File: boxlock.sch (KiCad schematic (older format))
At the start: 38 parts, among them J2 SOLENOID, J3 USB_B, J4 VEXT, J6 CONN_02X05, J8 KEYPAD, Q1 TIP120, Q2 TIP120, SW1 RESET, U1 LD1117AS33TR, U2 NE555, U3 SAMD21E

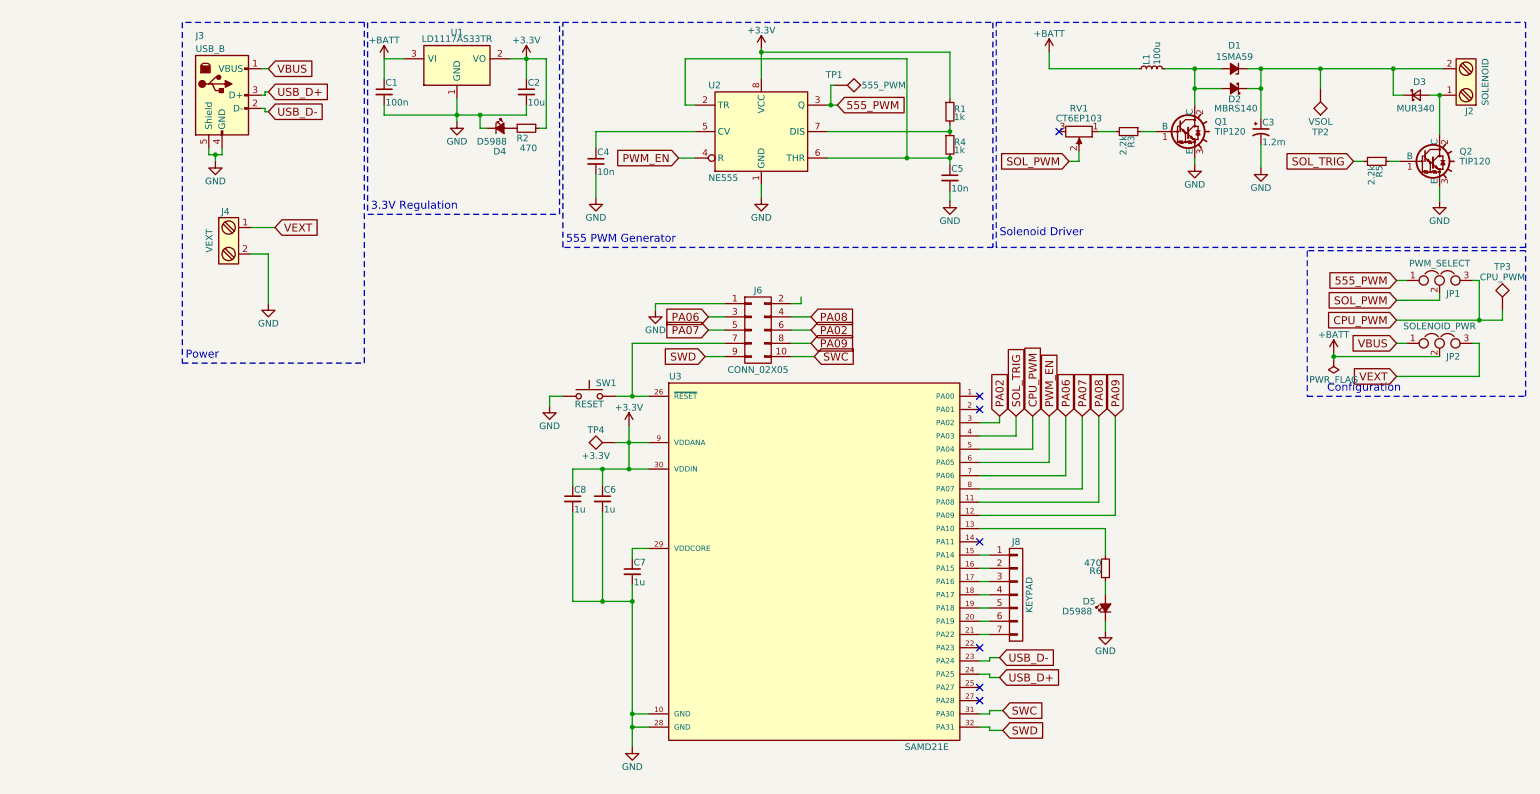
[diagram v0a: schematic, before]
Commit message: Relayout for rev 1.1.
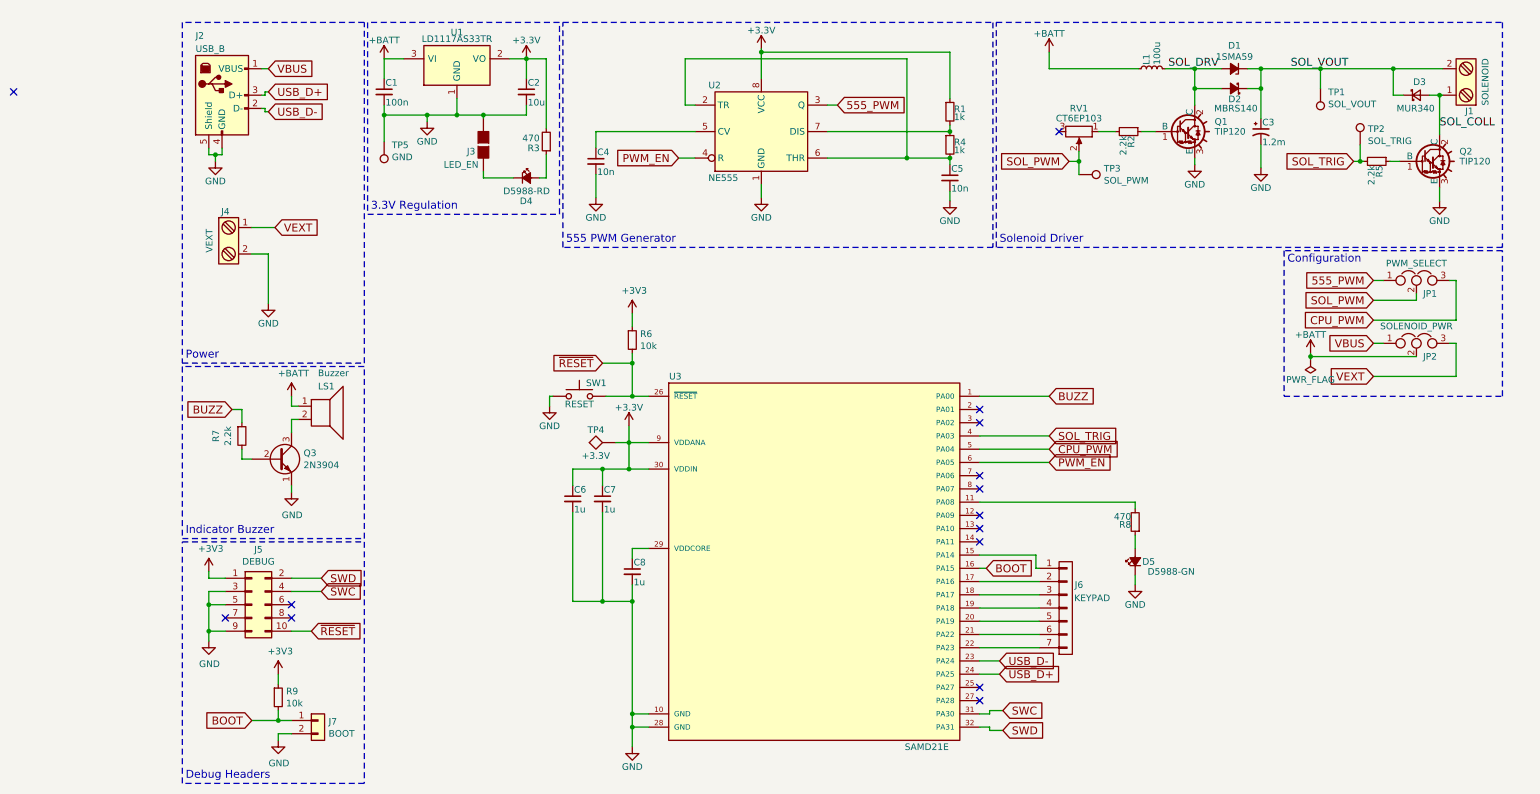
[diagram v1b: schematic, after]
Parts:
- removed J6: CONN_02X05, Pin_Headers:Pin_Header_Straight_2x05_Pitch2.54mm, symbol boxlock-rescue:CONN_02X05-RESCUE-boxlock
- removed TP1: 555_PWM, Measurement_Points:Test_Point_Keystone_5005-5009_Compact, symbol boxlock-rescue:TEST-RESCUE-boxlock
- removed TP2: VSOL, Measurement_Points:Test_Point_Keystone_5005-5009_Compact, symbol boxlock-rescue:TEST-RESCUE-boxlock
- removed TP3: CPU_PWM, Measurement_Points:Test_Point_Keystone_5005-5009_Compact, symbol boxlock-rescue:TEST-RESCUE-boxlock
- added J3: LED_EN, Connectors:GS2, symbol Connector:GS2
- added J5: DEBUG, Pin_Headers:Pin_Header_Straight_2x05_Pitch1.27mm, symbol Connector:Conn_02x05_Odd_Even
- added J7: BOOT, Pin_Headers:Pin_Header_Straight_1x02_Pitch2.54mm, symbol Connector:Conn_01x02
- added LS1: Buzzer, footprints:CEP-2242, symbol device:Speaker
- added Q3: 2N3904, TO_SOT_Packages_THT:TO-92_Molded_Narrow, symbol Transistor:2N3904
- added R6, R9: 10k, Resistors_SMD:R_0805_HandSoldering, symbol device:R_Small
- added R7: 2.2k, Resistors_SMD:R_0805_HandSoldering, symbol device:R_Small
- added TP1: SOL_VOUT, Measurement_Points:Test_Point_Keystone_5005-5009_Compact, symbol Connector:Test_Point
- added TP2: SOL_TRIG, Measurement_Points:Test_Point_Keystone_5005-5009_Compact, symbol Connector:Test_Point
- added TP3: SOL_PWM, Measurement_Points:Test_Point_Keystone_5005-5009_Compact, symbol Connector:Test_Point
- added TP5: GND, Measurement_Points:Test_Point_Keystone_5005-5009_Compact, symbol Connector:Test_Point
- D4: value D5988 -> D5988-RD
- D5: value D5988 -> D5988-GN
- J2: renamed from J3; footprint Connectors:USB_Micro-B -> footprints:USB_Micro-B-circular
- renumbered C8 to C6, C6 to C7, C7 to C8, J2 to J1, J8 to J6, R3 to R2, R2 to R3, R6 to R8
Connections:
- net PA08 is gone; now on an unnamed net: U3.11 (PA08)
- net +3V3: now also R3.2, J5.1 (Pin_1), R6.1, R9.1; no longer R3.1
- net +BATT: now also LS1.1
- net GND: now also J3.2 (G2), J5.3 (Pin_3), J5.5 (Pin_5), J5.9 (Pin_9), J7.2 (Pin_2), Q3.1 (E), TP5.1; no longer D4.1 (K)
- net SOL_PWM: now also TP3.1
- net SOL_TRIG: now also TP2.1
- net SWC: now also J5.4 (Pin_4)
- net SWD: now also J5.2 (Pin_2)
- net SOL_VOUT: now reaches C3.1, D1.1 (K), D2.1 (K), D3.1 (K), J1.2
- net SOL_VOUT: now also TP1.1
- net SOL_COLL: now reaches D3.2 (A), J1.1, Q2.2 (C)
- net SOL_DRV: now reaches D1.2 (A), D2.2 (A), L1.2, Q1.2 (C)
- net ~RESET: now reaches SW1.2, U3.26 (~RESET~)
- net ~RESET: now also J5.10 (Pin_10), R6.2
- net BUZZ: now reaches U3.1 (PA00)
- net BUZZ: now also R7.1
- net at R8.2: no longer U3.13 (PA10)
- net at J6.2 (P2): now also U3.17 (PA16); no longer U3.16 (PA15)
- net at J6.3 (P3): now also U3.18 (PA17); no longer U3.17 (PA16)
- net at J6.4 (P4): now also U3.19 (PA18); no longer U3.18 (PA17)
- net at J6.5 (P5): now also U3.20 (PA19); no longer U3.19 (PA18)
- net at J6.6 (P6): now also U3.21 (PA22); no longer U3.20 (PA19)
- net at J6.7 (P7): now also U3.22 (PA23); no longer U3.21 (PA22)
- net at D4.2 (A): now also R3.1; no longer R3.2
- net PA02: no longer names the net of U3.3 (PA02)
- net PA06: no longer names the net of U3.7 (PA06)
- net PA07: no longer names the net of U3.8 (PA07)
- net PA09: no longer names the net of U3.12 (PA09)
- new net: D4.1 (K), J3.1 (G1)
- new net: LS1.2, Q3.3 (C)
- new net: Q3.2 (B), R7.2
- new net BOOT: J7.1 (Pin_1), R9.2, U3.16 (PA15)
- no-connect marks 7 -> 14
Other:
- note added: "Debug Headers"
- note added: "Indicator Buzzer"
- moved on the sheet: D4, D5, J6, JP1, JP2, R3, R8, SW1

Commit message: Update to KiCAD 5.0.
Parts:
- C1, C2, C4, C5, C6, C7, C8: symbol device:C_Small -> Device:C_Small
- C3: symbol device:CP1_Small -> Device:CP1_Small
- D1: symbol device:D_Zener_Small_ALT -> Device:D_Zener_Small_ALT
- D2: symbol device:D_Schottky_Small_ALT -> Device:D_Schottky_Small_ALT
- D3: symbol device:D_Schottky_Small -> Device:D_Schottky_Small
- D4, D5: symbol device:LED_Small_ALT -> Device:LED_Small_ALT
- J3: footprint Connectors:GS2 -> Jumper:SolderJumper-2_P1.3mm_Open_Pad1.0x1.5mm; symbol Connector:GS2 -> Jumper:SolderJumper_2_Open
- J5: symbol Connector:Conn_02x05_Odd_Even -> Connector_Generic:Conn_02x05_Odd_Even
- J7: symbol Connector:Conn_01x02 -> Connector_Generic:Conn_01x02
- JP1, JP2: symbol device:Jumper_NC_Dual -> Device:Jumper_NC_Dual
- L1: symbol device:L_Small -> Device:L_Small
- LS1: symbol device:Speaker -> Device:Speaker
- Q3: symbol Transistor:2N3904 -> Transistor_BJT:2N3904
- R1, R2, R3, R4, R5, R6, R7, R8, R9: symbol device:R_Small -> Device:R_Small
- RV1: symbol device:POT -> Device:R_POT
- TP1, TP2, TP3, TP5: symbol Connector:Test_Point -> Connector:TestPoint
- U2: symbol linear:NE555 -> ltc6269:NE555
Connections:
- wire segments 150 -> 181
- no-connect marks 14 -> 13
